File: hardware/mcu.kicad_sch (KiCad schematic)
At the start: 26 parts, among them J201 Conn_ARM_JTAG_SWD_10, SW201 SW_Push, U201 EFR32FG28A122F1024GM48-A, U202 USBLC6-2P6, U203 USBLC6-2P6, Y201 LF_Crystal, Y202 ECS-390-CDX-1932

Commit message: fixed ERC issues
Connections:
- net BDE_RESET renamed BDE_RST
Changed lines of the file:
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@@
 		)
 	)
-	(hierarchical_label "BDE_RESET"
+	(hierarchical_label "BDE_RST"
 		(shape output)
 		(at 83.82 88.9 180)
@@
 					(unit 1)
 				)
+			)
+		)
+	)
+	(symbol
+		(lib_id "power:PWR_FLAG")
+		(at 246.38 41.91 270)
+		(unit 1)
+		(exclude_from_sim no)
+		(in_bom yes)
+		(on_board yes)
+		(dnp no)
+		(property "Reference" "#FLG0201"
+			(at 248.285 41.91 0)
+			(effects
+				(font
+					(size 1.27 1.27)
+				)
+				(hide yes)
+			)
+		)
+		(property "Value" "PWR_FLAG"
+			(at 247.65 44.704 90)
+			(effects
+				(font
+					(size 1.27 1.27)
+				)
+				(justify left)
+			)
+		)
+		(property "Footprint" ""
+			(at 246.38 41.91 0)
+			(effects
+				(font
+					(size 1.27 1.27)
+				)
+				(hide yes)
+			)
+		)
+		(property "Datasheet" "~"
+			(at 246.38 41.91 0)
+			(effects
+				(font
+					(size 1.27 1.27)
+				)
+				(hide yes)
+			)
+		)
+		(property "Description" "Special symbol for telling ERC where power comes from"
+			(at 246.38 41.91 0)
+			(effects
+				(font
+					(size 1.27 1.27)
+				)
+				(hide yes)
+			)
+		)
+		(pin "1"
+		)
+		(instances
+			(project ""
+				(path "/8f5928e8-0fc1-4443-a20f-3bfeb956761e/eaf224bf-a12f-4d12-aa0a-28551b47d007"
+					(reference "#FLG0201")
+					(unit 1)
+				)

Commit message: reannotate
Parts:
- renumbered C201 to C101, C202 to C102, C203 to C103, C204 to C104, C205 to C105, C206 to C106, C207 to C107, C208 to C108, C209 to C109, D201 to D101, D202 to D102, D203 to D103, D204 to D104, J201 to J101, R201 to R101, R202 to R102, R203 to R103, R204 to R104, R205 to R105, R206 to R106, SW201 to SW101, U201 to U101, U202 to U102, U203 to U103, Y201 to Y101, Y202 to Y102

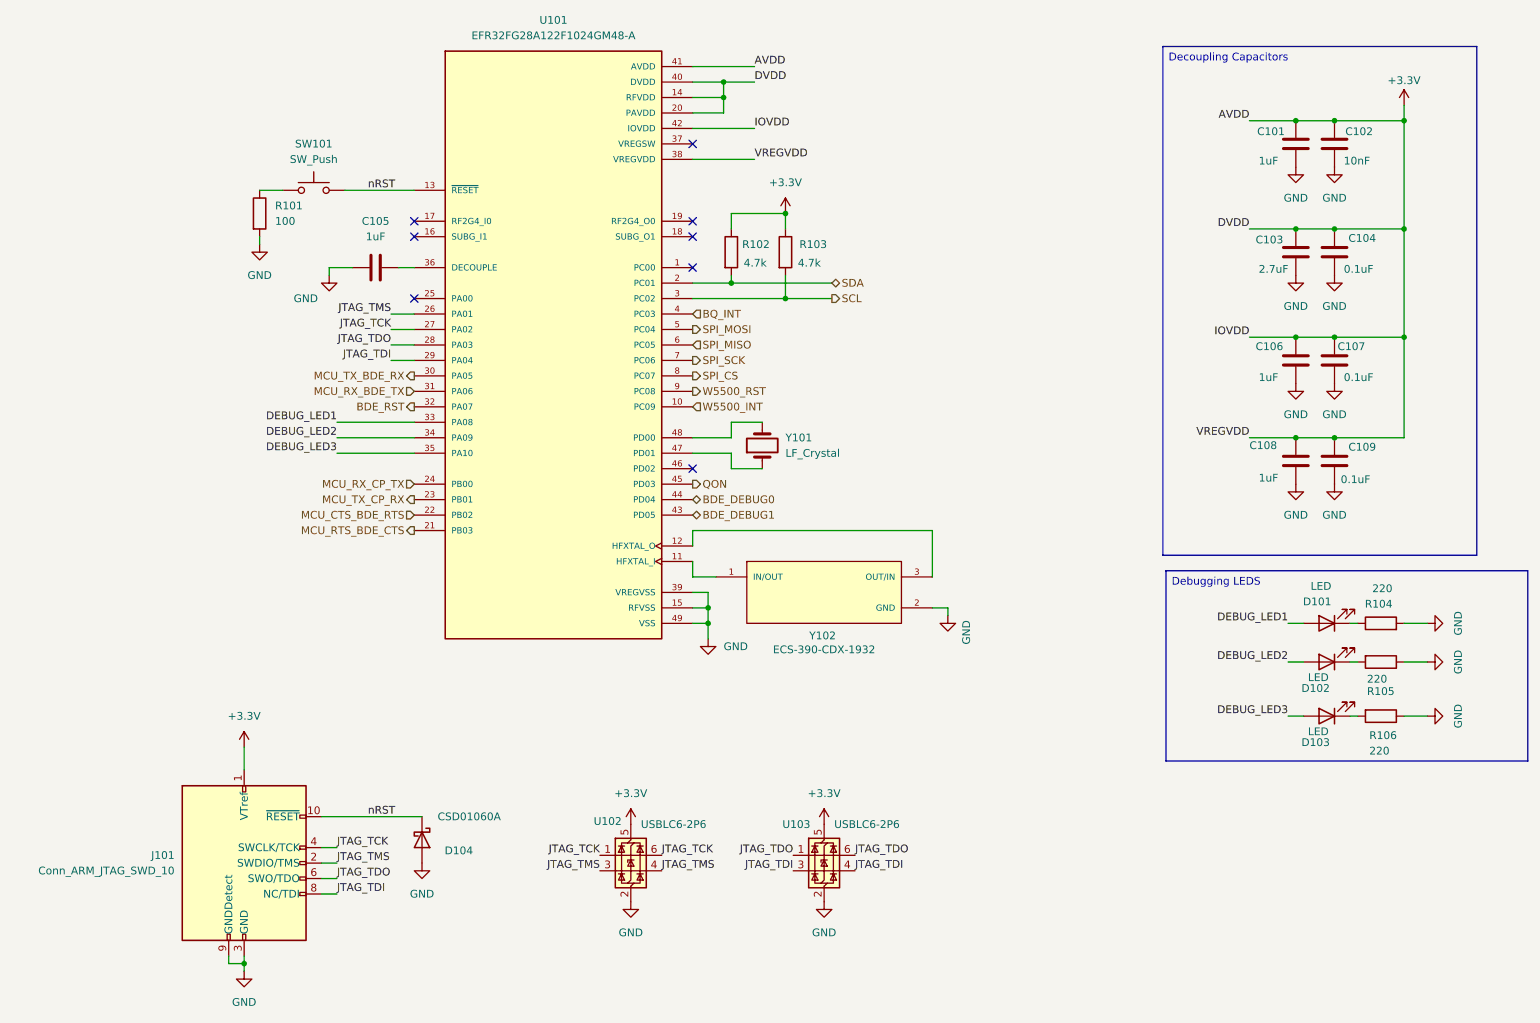
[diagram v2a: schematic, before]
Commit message: added QON pushbutton
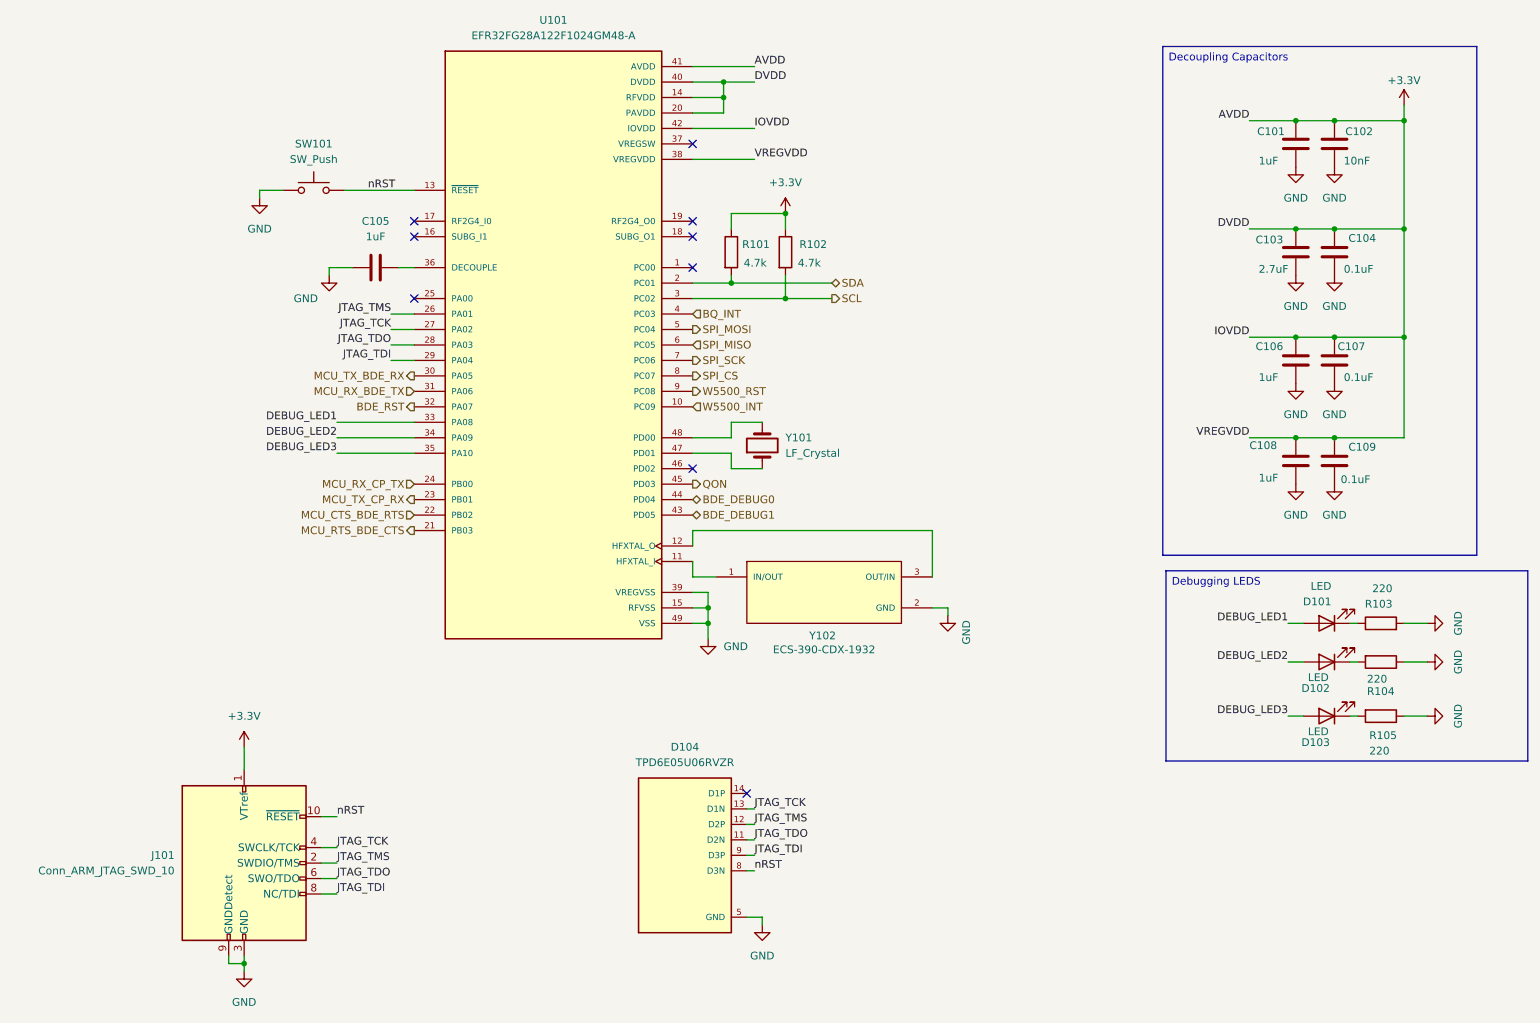
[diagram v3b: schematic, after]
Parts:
- removed D104: CSD01060A, Diode_SMD:D_SOD-123, symbol Diode:CSD01060A
- removed R101: 100, Resistor_SMD:R_0805_2012Metric, symbol Device:R
- removed U102, U103: USBLC6-2P6, Package_TO_SOT_SMD:SOT-666, symbol Power_Protection:USBLC6-2P6
- added D104: TPD6E05U06RVZR, pyronet_footprints:SON50P135X350X55-14N, symbol pyronet_symbols:TPD6E05U06RVZR
- renumbered R102 to R101, R103 to R102, R104 to R103, R105 to R104, R106 to R105
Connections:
- net GND: now also SW101.1, D104.10 (GND), D104.5 (GND)
- net JTAG_TCK: now also D104.13 (D1N)
- net JTAG_TDI: now also D104.9 (D3P)
- net JTAG_TDO: now also D104.11 (D2N)
- net JTAG_TMS: now also D104.12 (D2P)
- net nRST: now also D104.8 (D3N)
- no-connect marks 8 -> 9

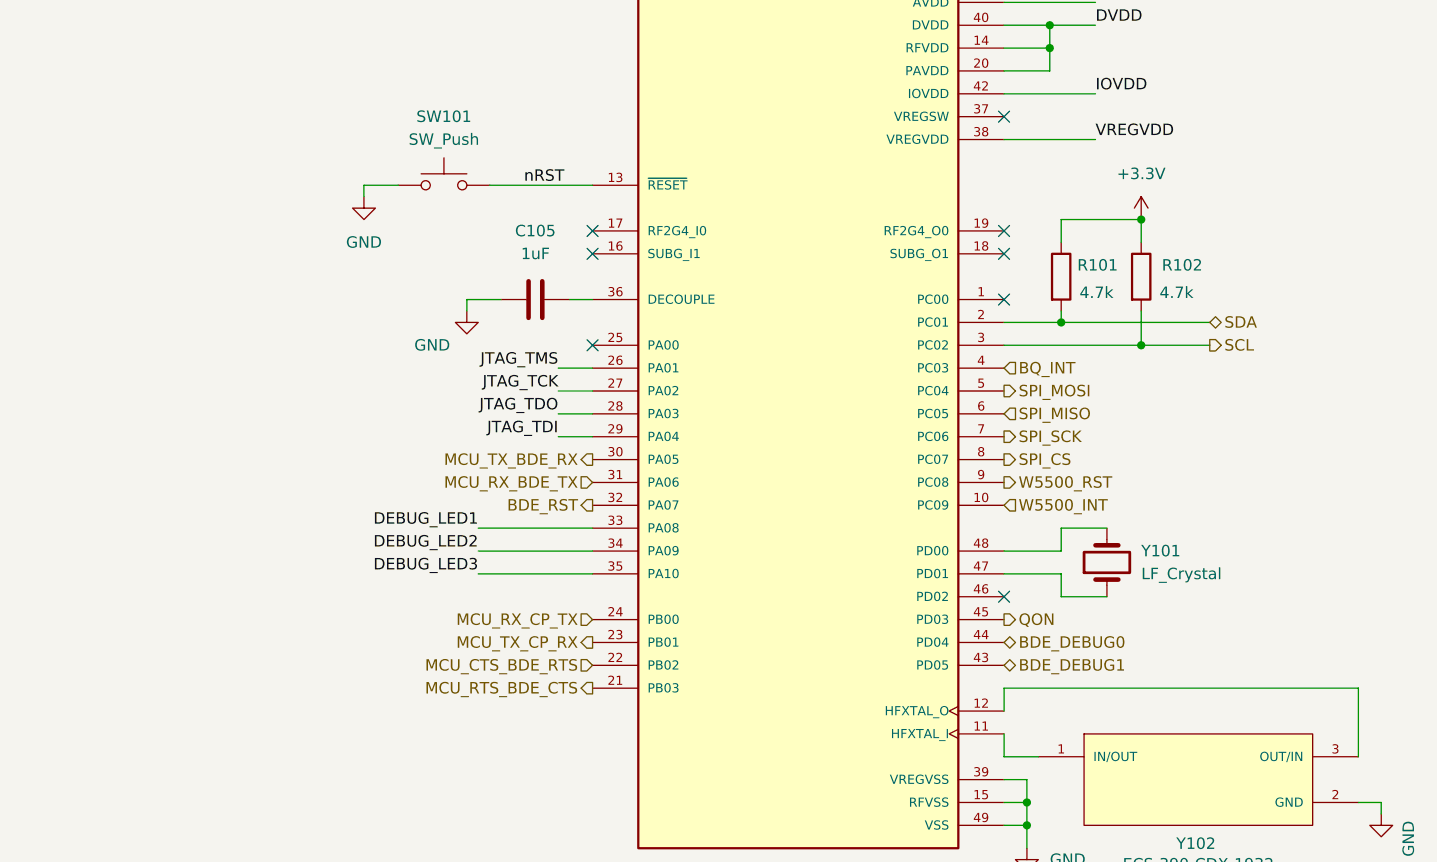
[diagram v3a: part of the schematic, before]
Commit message: MCU pin reassignment
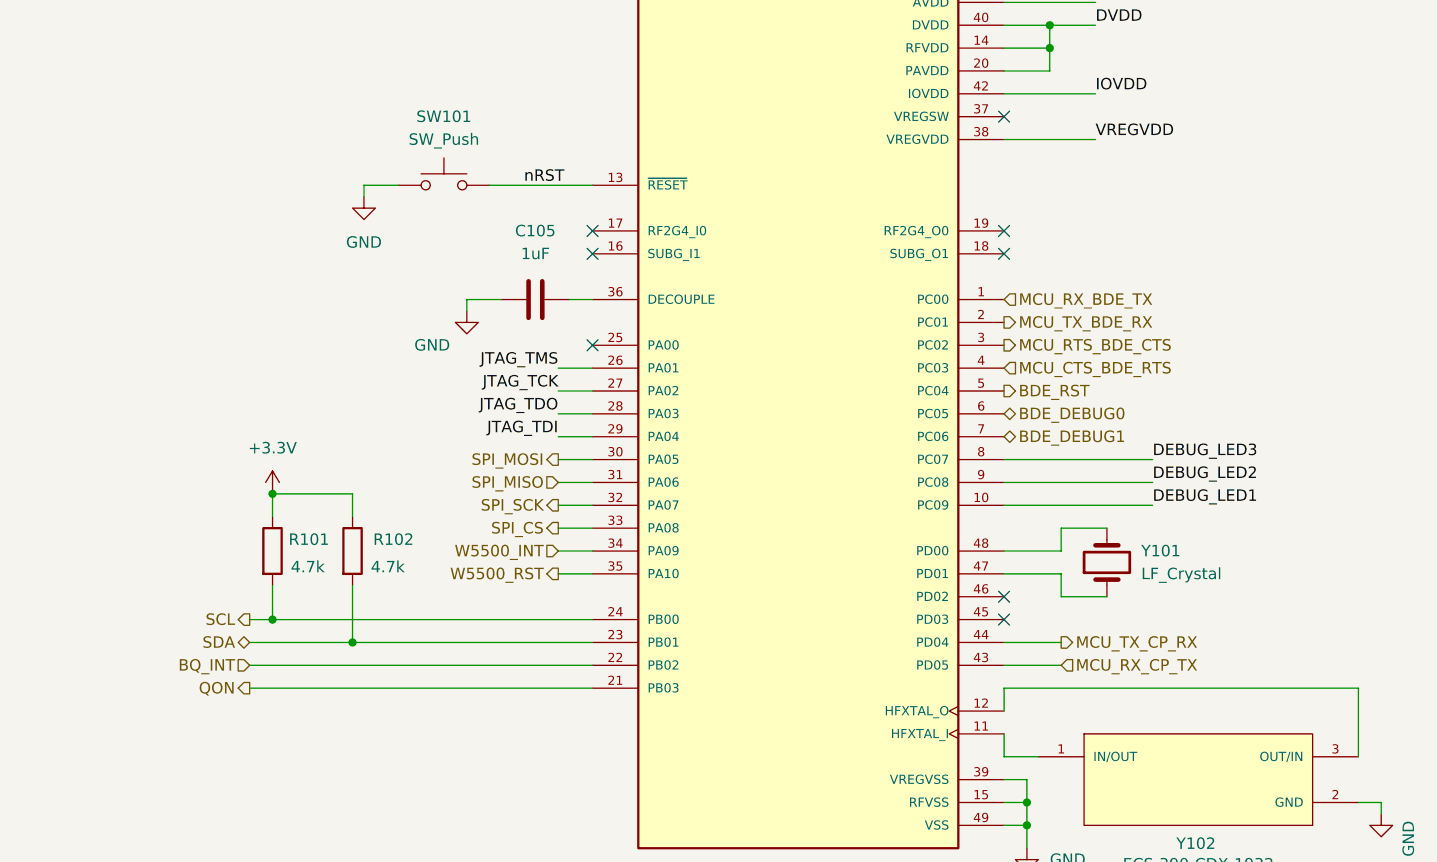
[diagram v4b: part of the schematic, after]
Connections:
- net BDE_DEBUG0: now also U101.6 (PC05); no longer U101.44 (PD04)
- net BDE_DEBUG1: now also U101.7 (PC06); no longer U101.43 (PD05)
- net BDE_RST: now also U101.5 (PC04); no longer U101.32 (PA07)
- net BQ_INT: now also U101.22 (PB02); no longer U101.4 (PC03)
- net DEBUG_LED1: now also U101.10 (PC09); no longer U101.33 (PA08)
- net DEBUG_LED2: now also U101.9 (PC08); no longer U101.34 (PA09)
- net DEBUG_LED3: now also U101.8 (PC07); no longer U101.35 (PA10)
- net MCU_CTS_BDE_RTS: now also U101.4 (PC03); no longer U101.22 (PB02)
- net MCU_RTS_BDE_CTS: now also U101.3 (PC02); no longer U101.21 (PB03)
- net MCU_RX_BDE_TX: now also U101.1 (PC00); no longer U101.31 (PA06)
- net MCU_RX_CP_TX: now also U101.43 (PD05); no longer U101.24 (PB00)
- net MCU_TX_BDE_RX: now also U101.2 (PC01); no longer U101.30 (PA05)
- net MCU_TX_CP_RX: now also U101.44 (PD04); no longer U101.23 (PB01)
- net QON: now also U101.21 (PB03); no longer U101.45 (PD03)
- net SCL: now also R101.2, U101.24 (PB00); no longer R102.2, U101.3 (PC02)
- net SDA: now also R102.2, U101.23 (PB01); no longer R101.2, U101.2 (PC01)
- net SPI_CS: now also U101.33 (PA08); no longer U101.8 (PC07)
- net SPI_MISO: now also U101.31 (PA06); no longer U101.6 (PC05)
- net SPI_MOSI: now also U101.30 (PA05); no longer U101.5 (PC04)
- net SPI_SCK: now also U101.32 (PA07); no longer U101.7 (PC06)
- net W5500_INT: now also U101.34 (PA09); no longer U101.10 (PC09)
- net W5500_RST: now also U101.35 (PA10); no longer U101.9 (PC08)
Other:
- moved on the sheet: R101, R102

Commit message: MCU pin update
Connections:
- net BQ_INT: now also U101.44 (PD04); no longer U101.22 (PB02)
- net MCU_RX_CP_TX: now also U101.22 (PB02); no longer U101.43 (PD05)
- net MCU_TX_CP_RX: now also U101.21 (PB03); no longer U101.44 (PD04)
- net QON: now also U101.43 (PD05); no longer U101.21 (PB03)
- net SCL: now also R102.2, U101.45 (PD03); no longer R101.2, U101.24 (PB00)
- net SDA: now also R101.2, U101.46 (PD02); no longer R102.2, U101.23 (PB01)
- net SPI_CS: now also U101.35 (PA10); no longer U101.33 (PA08)
- net SPI_MISO: now also U101.33 (PA08); no longer U101.31 (PA06)
- net SPI_MOSI: now also U101.32 (PA07); no longer U101.30 (PA05)
- net SPI_SCK: now also U101.34 (PA09); no longer U101.32 (PA07)
- net W5500_INT: now also U101.24 (PB00); no longer U101.34 (PA09)
- net W5500_RST: now also U101.23 (PB01); no longer U101.35 (PA10)
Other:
- moved on the sheet: R101, R102, Y101

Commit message: Merge .kicad_sch schematic updates from diego-pcb
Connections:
- net BDE_DEBUG0: now also U101.5 (PC04); no longer U101.6 (PC05)
- net BDE_DEBUG1: now also U101.6 (PC05); no longer U101.7 (PC06)
- net BDE_RST: now also U101.7 (PC06); no longer U101.5 (PC04)
- net BQ_INT: now also U101.43 (PD05); no longer U101.44 (PD04)
- net MCU_RX_CP_TX: now also U101.34 (PA09); no longer U101.22 (PB02)
- net MCU_TX_CP_RX: now also U101.35 (PA10); no longer U101.21 (PB03)
- net QON: now also U101.44 (PD04); no longer U101.43 (PD05)
- net SCL: now also R101.2, U101.46 (PD02); no longer R102.2, U101.45 (PD03)
- net SDA: now also R102.2, U101.45 (PD03); no longer R101.2, U101.46 (PD02)
- net SPI_CS: now also U101.24 (PB00); no longer U101.35 (PA10)
- net SPI_MISO: now also U101.22 (PB02); no longer U101.33 (PA08)
- net SPI_MOSI: now also U101.21 (PB03); no longer U101.32 (PA07)
- net SPI_SCK: now also U101.23 (PB01); no longer U101.34 (PA09)
- net W5500_INT: now also U101.31 (PA06); no longer U101.24 (PB00)
- net W5500_RST: now also U101.32 (PA07); no longer U101.23 (PB01)

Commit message: BMS layout
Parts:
- added NT101, NT102, NT103, NT104: NetTie_2, symbol Device:NetTie_2
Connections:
- net +3.3V: now also NT101.2, NT102.2, NT103.2, NT104.2; no longer C101.1, C102.1, C103.1, C104.1, C106.1, C107.1, C108.1, C109.1, U101.14 (RFVDD), U101.20 (PAVDD), U101.38 (VREGVDD), U101.40 (DVDD), U101.41 (AVDD), U101.42 (IOVDD)
- net MCU_RX_CP_TX: now also U101.33 (PA08); no longer U101.34 (PA09)
- net MCU_TX_CP_RX: now also U101.34 (PA09); no longer U101.35 (PA10)
- new net AVDD: C101.1, C102.1, NT101.1, U101.41 (AVDD)
- new net DVDD: C103.1, C104.1, NT102.1, U101.14 (RFVDD), U101.20 (PAVDD), U101.40 (DVDD)
- new net IOVDD: C106.1, C107.1, NT103.1, U101.42 (IOVDD)
- new net PS_SYNC: U101.35 (PA10)
- new net VREGVDD: C108.1, C109.1, NT104.1, U101.38 (VREGVDD)
- no-connect marks 9 -> 8

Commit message: BMS layout
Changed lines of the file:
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@@
-		)
-	)
-	(hierarchical_label "PS_SYNC"
-		(shape input)
-		(at 62.23 101.6 180)
-		(effects
-			(font
-				(size 1.27 1.27)
-			)
-			(justify right)
 		)
 	)
